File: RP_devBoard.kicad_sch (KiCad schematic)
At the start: 14 parts, among them J1 Conn_01x04, J2 Conn_01x04, J3 TC2030, J4 TC2030, J5 USB_C_Receptacle, J6 USB_C_Receptacle, U3 BME280, U4 NCP1117-3.3_SOT223

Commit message: Adding source, source control
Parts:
- removed C1, C2: 10uF, Capacitor_SMD:C_0603_1608Metric, symbol Device:C
- removed J1, J2: Conn_01x04, Connector_JST:JST_SH_BM04B-SRSS-TB_1x04-1MP_P1.00mm_Vertical, symbol Connector_Generic:Conn_01x04
- removed J3, J4: TC2030, Connector:Tag-Connect_TC2030-IDC-NL_2x03_P1.27mm_Vertical, symbol Connector:TC2030
- removed J5, J6: USB_C_Receptacle, Connector_USB:USB_C_Receptacle_Amphenol_12401610E4-2A, symbol Connector:USB_C_Receptacle
- removed R1, R11, R12, R2: 5.1k, Resistor_SMD:R_0603_1608Metric, symbol Device:R
- removed U4: NCP1117-3.3_SOT223, Package_TO_SOT_SMD:SOT-223-3_TabPin2, symbol Regulator_Linear:NCP1117-3.3_SOT223
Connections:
- no-connect marks 20 -> 0
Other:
- added sheet COM_PORTS (modules/COM_PORTS.kicad_sch)
- sheet ESP32 ports: added ESP_BOOT, ESP_RESET, ESP_RX, ESP_TX; removed none
- sheet RP2350B ports: added RPB_I2C_SCL, RPB_I2C_SDA, RPB_SWO; removed none
- moved on the sheet: U3

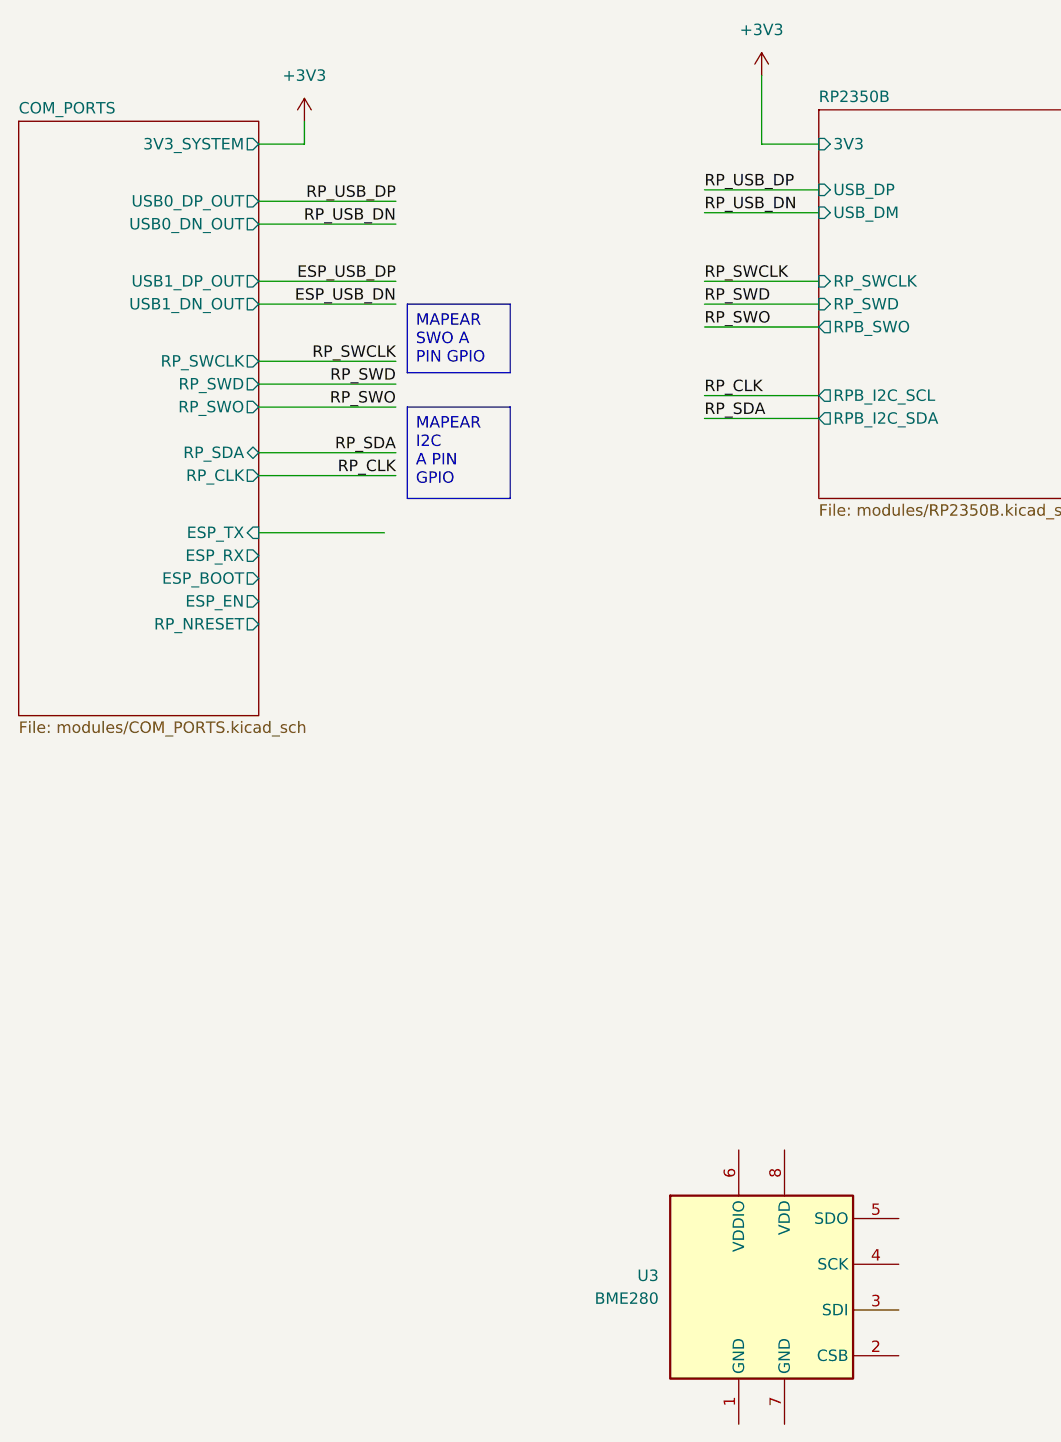
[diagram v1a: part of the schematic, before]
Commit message: Adding mikroBUS
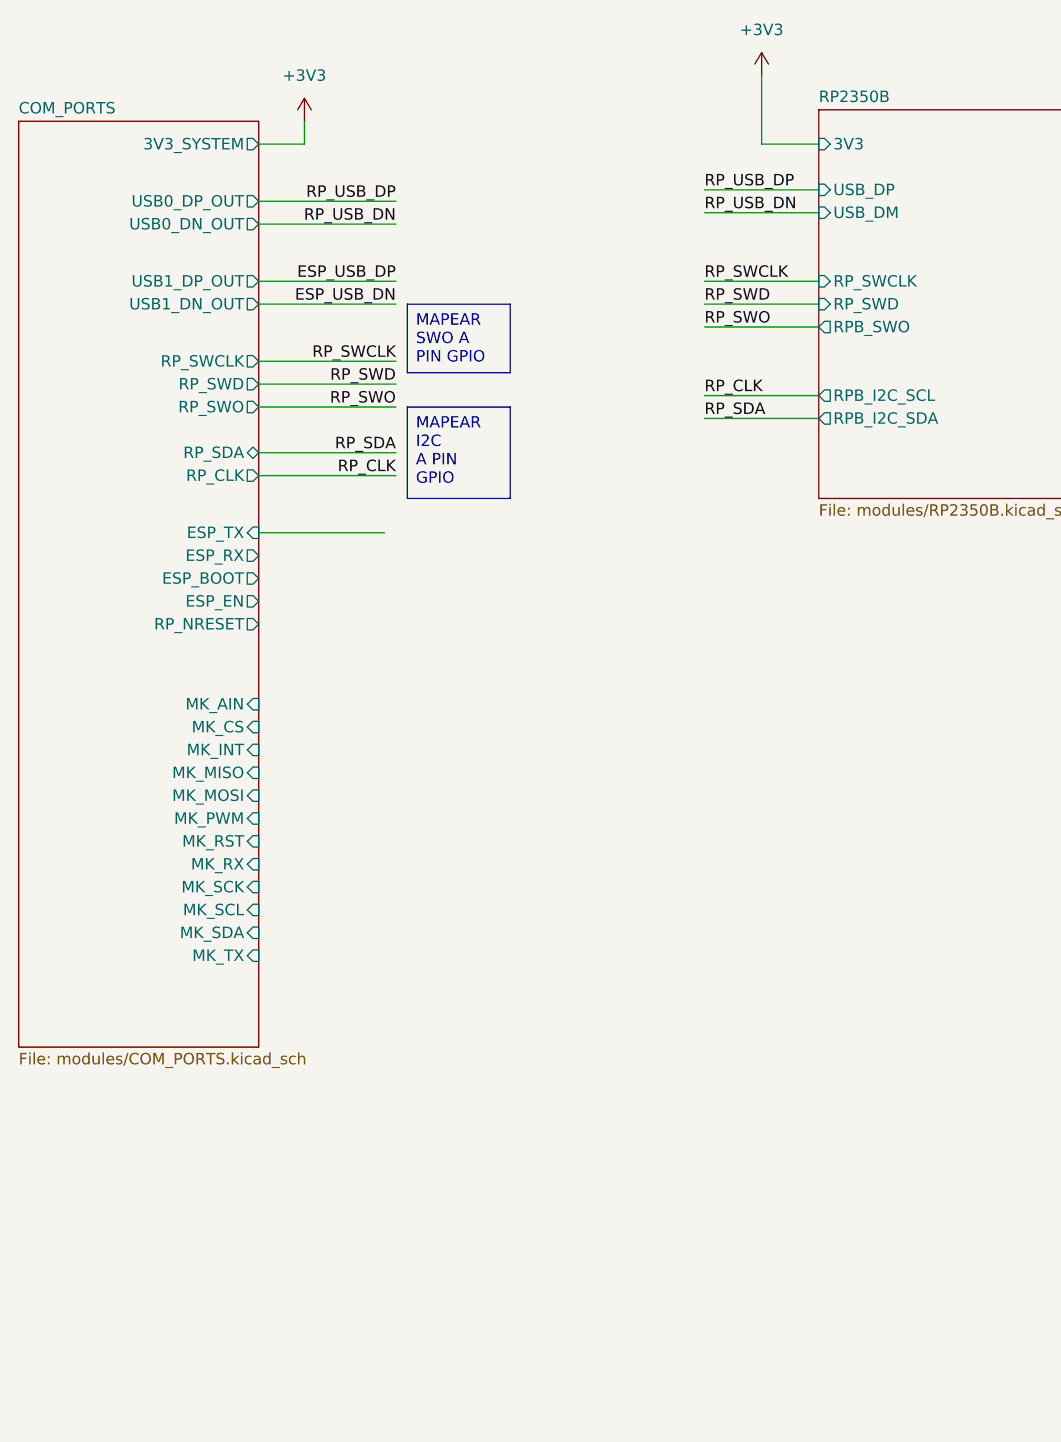
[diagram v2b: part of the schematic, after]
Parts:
- removed U3: BME280, Package_LGA:Bosch_LGA-8_2.5x2.5mm_P0.65mm_ClockwisePinNumbering, symbol Sensor:BME280
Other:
- sheet COM_PORTS ports: added MK_AIN, MK_CS, MK_INT, MK_MISO, MK_MOSI, MK_PWM, MK_RST, MK_RX, MK_SCK, MK_SCL, MK_SDA, MK_TX; removed none
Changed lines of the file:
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@@
-	)
-	(symbol
-		(lib_id "Sensor:BME280")
-		(at 106.68 161.29 0)
-		(unit 1)
-		(exclude_from_sim no)
-		(in_bom yes)
-		(on_board yes)
-		(dnp no)
-		(fields_autoplaced yes)
-		(property "Reference" "U3"
-			(at 95.25 160.0199 0)
-			(effects
-				(font
-					(size 1.27 1.27)
-				)
-				(justify right)
-			)
-		)
-		(property "Value" "BME280"
-			(at 95.25 162.5599 0)
-			(effects
-				(font
-					(size 1.27 1.27)
-				)
-				(justify right)
-			)
-		)
-		(property "Footprint" "Package_LGA:Bosch_LGA-8_2.5x2.5mm_P0.65mm_ClockwisePinNumbering"
-			(at 144.78 172.72 0)
-			(effects
-				(font
-					(size 1.27 1.27)
-				)
-				(hide yes)
-			)
-		)
-		(property "Datasheet" "https://www.bosch-sensortec.com/media/boschsensortec/downloads/datasheets/bst-bme280-ds002.pdf"
-			(at 106.68 166.37 0)
-			(effects
-				(font
-					(size 1.27 1.27)
-				)
-				(hide yes)
-			)
-		)
-		(property "Description" "3-in-1 sensor, humidity, pressure, temperature, I2C and SPI interface, 1.71-3.6V, LGA-8"
-			(at 106.68 161.29 0)
-			(effects
-				(font
-					(size 1.27 1.27)
-				)
-				(hide yes)
-			)
-		)
-		(property "Part Number" ""
-			(at 106.68 161.29 0)
-			(effects
-				(font
-					(size 1.27 1.27)
-				)
-				(hide yes)
-			)
-		)
-		(property "Provider" ""
-			(at 106.68 161.29 0)
-			(effects
-				(font
-					(size 1.27 1.27)
-				)
-				(hide yes)
-			)
-		)
-		(pin "2"
-		)
-		(pin "8"
-		)
-		(pin "7"
-		)
-		(pin "5"
-		)
-		(pin "4"
-		)
-		(pin "3"
-		)
-		(pin "6"
-		)
-		(pin "1"
-		)
-		(instances
-			(project ""
-				(path "/3efb3214-cf20-4475-a403-c426a77bfef6"
-					(reference "U3")
-					(unit 1)
-				)
-			)
-		)
 	)
 	(symbol
@@
 	(sheet
 		(at 24.13 31.75)
-		(size 26.67 66.04)
+		(size 26.67 102.87)
 		(exclude_from_sim no)
 		(in_bom yes)
@@
 		)
 		(property "Sheetfile" "modules/COM_PORTS.kicad_sch"
-			(at 24.13 98.3746 0)
+			(at 24.13 135.2046 0)
 			(effects
 				(font
@@
 			(effects
 				(font
+					(size 1.27 1.27)
+				)
+				(justify right)
+			)
+		)
+		(pin "MK_AIN" input
+			(at 50.8 96.52 0)
+			(effects
+				(font
+					(size 1.27 1.27)
+				)
+				(justify right)
+			)
+		)
+		(pin "MK_CS" input
+			(at 50.8 99.06 0)
+			(effects
+				(font
+					(size 1.27 1.27)
+				)
+				(justify right)
+			)
+		)
+		(pin "MK_INT" input
+			(at 50.8 101.6 0)
+			(effects
+				(font
+					(size 1.27 1.27)
+				)
+				(justify right)
+			)
+		)
+		(pin "MK_MISO" input
+			(at 50.8 104.14 0)
+			(effects
+				(font
+					(size 1.27 1.27)
+				)
+				(justify right)
+			)
+		)
+		(pin "MK_MOSI" input
+			(at 50.8 106.68 0)
+			(effects
+				(font
+					(size 1.27 1.27)
+				)
+				(justify right)
+			)
+		)
+		(pin "MK_PWM" input
+			(at 50.8 109.22 0)
+			(effects
+				(font
+					(size 1.27 1.27)
+				)
+				(justify right)
+			)
+		)
+		(pin "MK_RST" input
+			(at 50.8 111.76 0)
+			(effects
+				(font
+					(size 1.27 1.27)
+				)
+				(justify right)
+			)
+		)
+		(pin "MK_RX" input
+			(at 50.8 114.3 0)
+			(effects
+				(font
+					(size 1.27 1.27)
+				)
+				(justify right)
+			)
+		)
+		(pin "MK_SCK" input
+			(at 50.8 116.84 0)
+			(effects
+				(font
+					(size 1.27 1.27)
+				)
+				(justify right)
+			)
+		)
+		(pin "MK_SCL" input
+			(at 50.8 119.38 0)
+			(effects
+				(font
+					(size 1.27 1.27)
+				)
+				(justify right)
+			)
+		)
+		(pin "MK_SDA" input
+			(at 50.8 121.92 0)
+			(effects
+				(font
+					(size 1.27 1.27)
+				)
+				(justify right)
+			)
+		)
+		(pin "MK_TX" input
+			(at 50.8 124.46 0)
+			(effects
+				(font

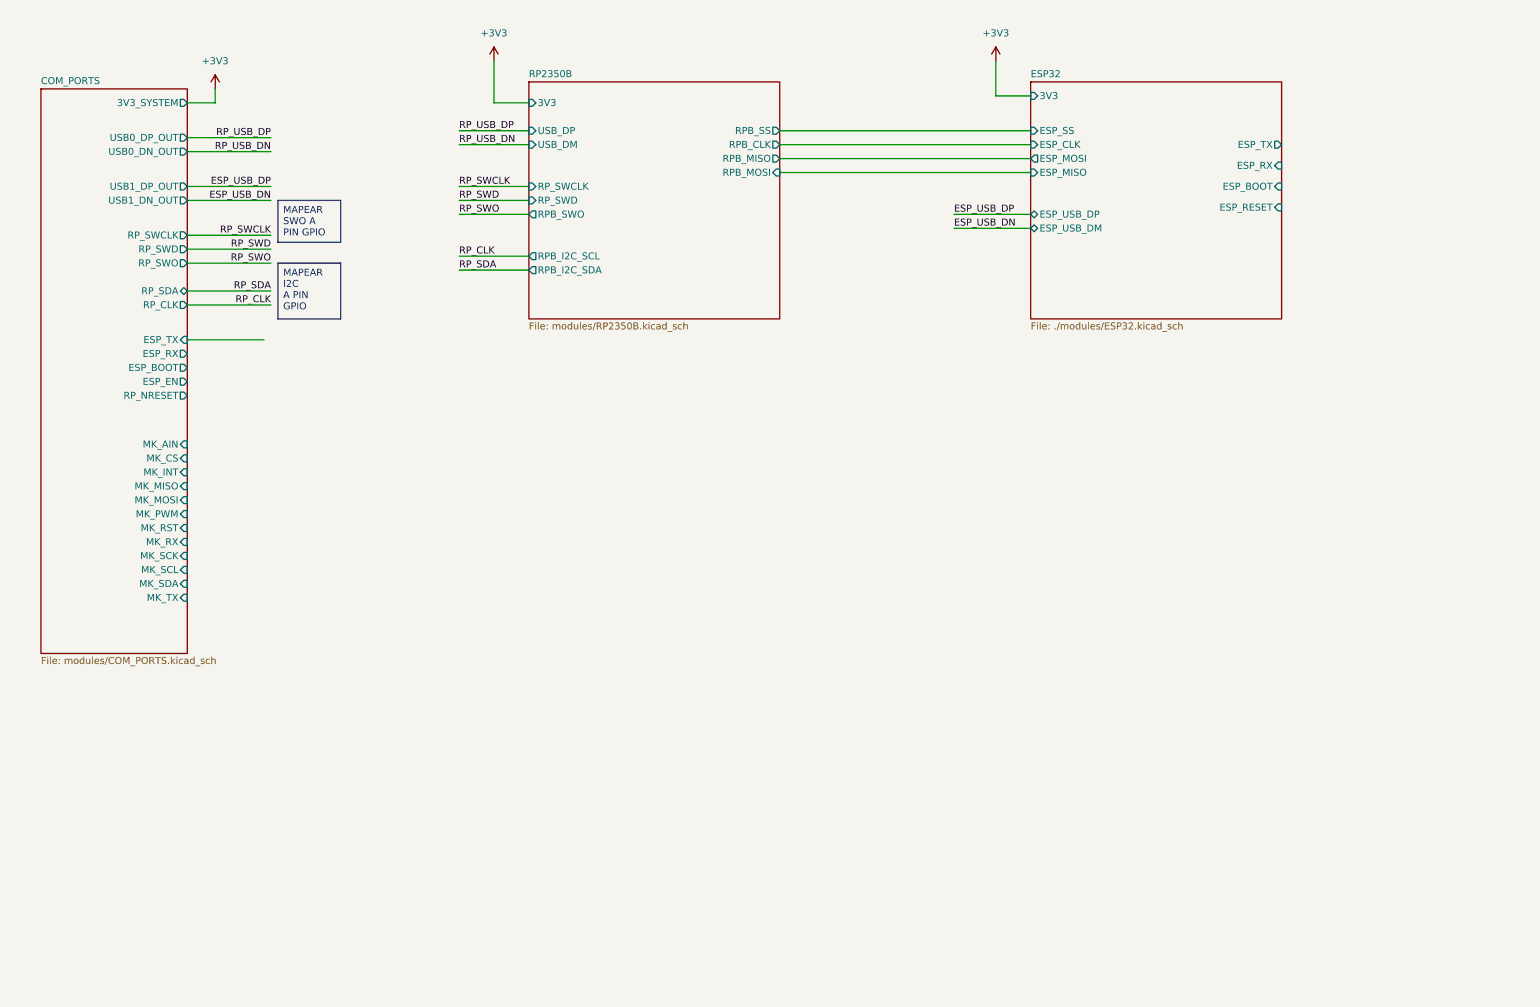
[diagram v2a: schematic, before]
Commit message: Modificaciond de conexiones
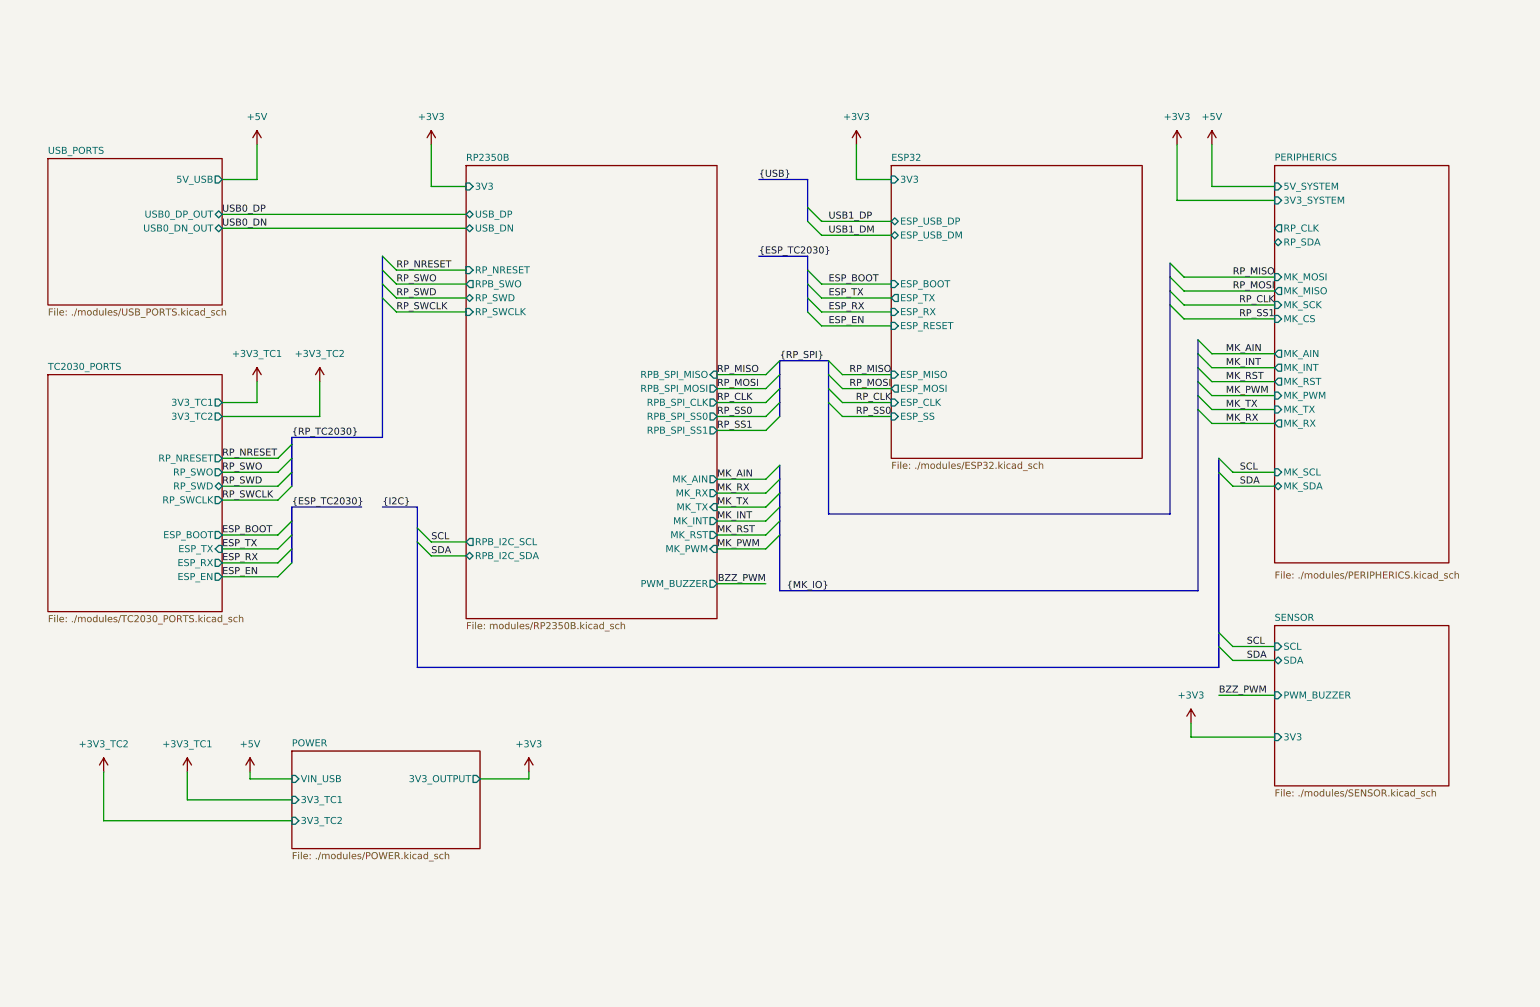
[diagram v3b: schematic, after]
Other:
- removed sheet COM_PORTS
- added sheet PERIPHERICS (./modules/PERIPHERICS.kicad_sch)
- added sheet POWER (./modules/POWER.kicad_sch)
- added sheet SENSOR (./modules/SENSOR.kicad_sch)
- added sheet TC2030_PORTS (./modules/TC2030_PORTS.kicad_sch)
- added sheet USB_PORTS (./modules/USB_PORTS.kicad_sch)
- sheet RP2350B ports: added MK_AIN, MK_INT, MK_PWM, MK_RST, MK_RX, MK_TX, PWM_BUZZER, RPB_SPI_CLK, RPB_SPI_MISO, RPB_SPI_MOSI, RPB_SPI_SS0, RPB_SPI_SS1, RP_NRESET, USB_DN; removed RPB_CLK, RPB_MISO, RPB_MOSI, RPB_SS, USB_DM
